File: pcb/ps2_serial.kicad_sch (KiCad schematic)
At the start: 37 parts, among them J1 Jumper 1, J2 Conn_01x06, J3 serial header, J4 SPI, J5 USB_A, J6 power, Q1 Q_PMOS_GDS, U1 ATtiny2313-20P, U2 MAX232, Y1 Crystal_Small

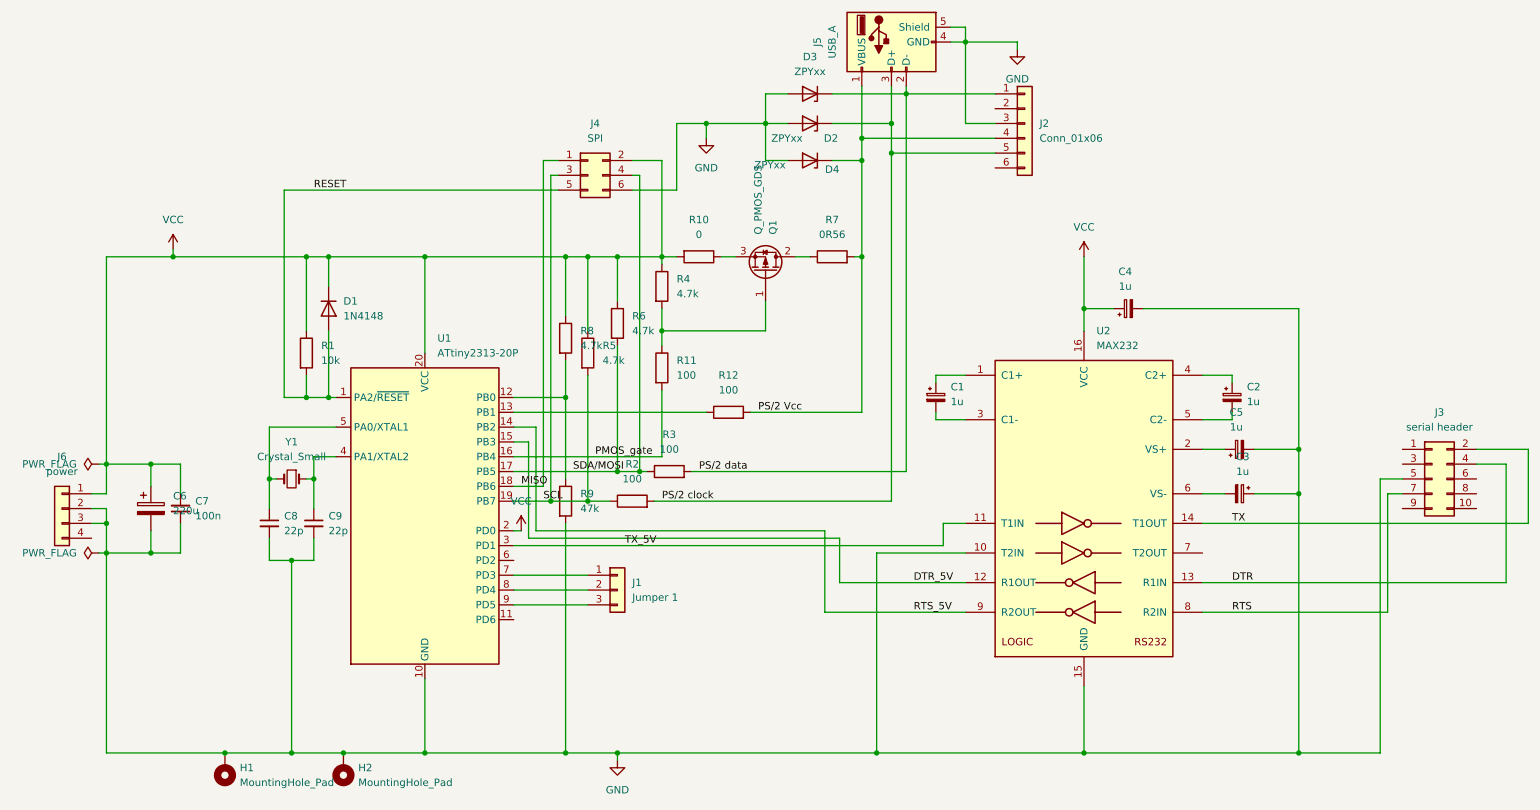
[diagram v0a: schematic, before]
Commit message: V2 for PCB. Implemented following changes: -more elegant mounting mechanism -more jumper settings -footprint for both USB and PS/2 socket -reservation for using INT0 to trigger SDA sampling -smaller size board
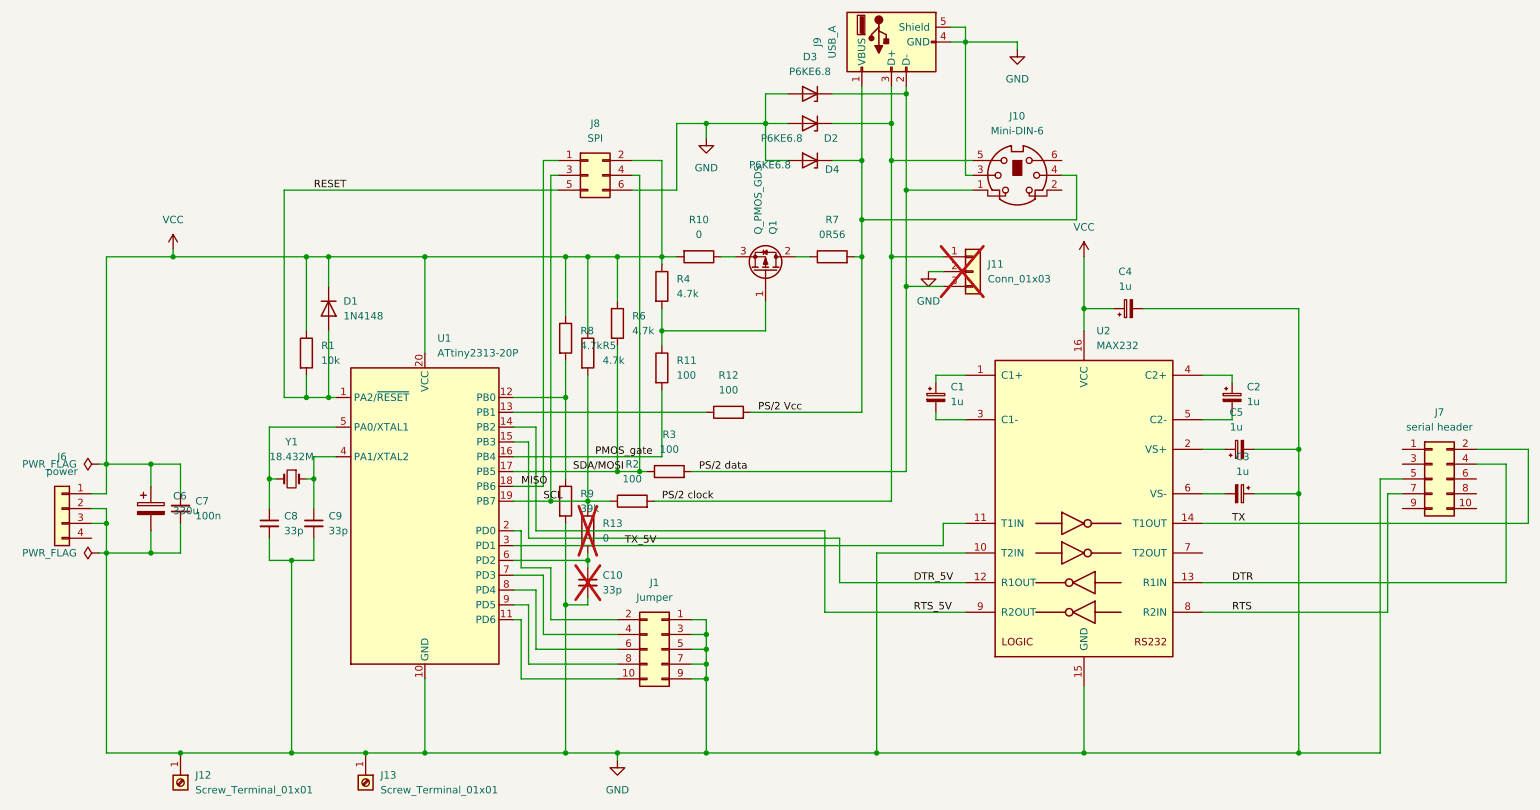
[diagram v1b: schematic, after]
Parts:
- removed H1, H2: MountingHole_Pad, MountingHole:MountingHole_4.3mm_M4_DIN965_Pad, symbol Mechanical:MountingHole_Pad
- removed J1: Jumper 1, Connector_PinHeader_2.54mm:PinHeader_1x03_P2.54mm_Vertical, symbol Connector_Generic:Conn_01x03
- removed J2: Conn_01x06, Connector_PinHeader_2.54mm:PinHeader_1x06_P2.54mm_Vertical, symbol Connector_Generic:Conn_01x06
- added C10: 33p, Capacitor_THT:C_Disc_D4.3mm_W1.9mm_P5.00mm, symbol Device:C_Small
- added J1: Jumper, Connector_PinHeader_2.54mm:PinHeader_2x05_P2.54mm_Vertical, symbol Connector_Generic:Conn_02x05_Odd_Even
- added J10: Mini-DIN-6, kicad:J_Mini-DIN-6, symbol Connector:Mini-DIN-6
- added J11: Conn_01x03, Connector_PinHeader_2.54mm:PinHeader_1x03_P2.54mm_Vertical, symbol Connector_Generic:Conn_01x03
- added J12, J13: Screw_Terminal_01x01, Amphenol:Amphenol_M4-44051DB, symbol Connector:Screw_Terminal_01x01
- added R13: 0, Resistor_THT:R_Axial_DIN0207_L6.3mm_D2.5mm_P10.16mm_Horizontal, symbol Device:R
- C6: value 220u -> 330u; footprint Capacitor_THT:CP_Radial_D10.0mm_P5.00mm -> Capacitor_THT:CP_Radial_D8.0mm_P3.50mm
- C8, C9: value 22p -> 33p
- D2, D3, D4: value ZPYxx -> P6KE6.8
- Q1: footprint Package_TO_SOT_SMD:TO-263-2 -> Package_TO_SOT_SMD:TO-252-2
- R9: value 47k -> 39k
- Y1: value Crystal_Small -> 18.432M
- renumbered J3 to J7, J4 to J8, J5 to J9
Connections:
- net GND: now also C10.2, J1.1 (Pin_1), J1.3 (Pin_3), J1.5 (Pin_5), J1.7 (Pin_7), J1.9 (Pin_9), J10.3, J11.2 (Pin_2), J12.1 (Pin_1), J13.1 (Pin_1)
- net PS/2 Vcc: now also J10.4
- net PS/2 clock: now also J10.5, J11.1 (Pin_1)
- net PS/2 data: now also J10.1, J11.3 (Pin_3)
- net SCL: now also R13.1
- net VCC: no longer U1.2 (PD0)
- net at U1.7 (PD3): now also J1.4 (Pin_4)
- net at U1.8 (PD4): now also J1.6 (Pin_6)
- net at U1.9 (PD5): now also J1.8 (Pin_8)
- net at U1.11 (PD6): now also J1.10 (Pin_10)
- net at U1.6 (PD2): now also C10.1, R13.2
- new net: J1.2 (Pin_2), U1.2 (PD0)
